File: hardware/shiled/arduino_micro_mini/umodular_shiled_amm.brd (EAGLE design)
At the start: 49.8 x 100.1 mm, 22 parts

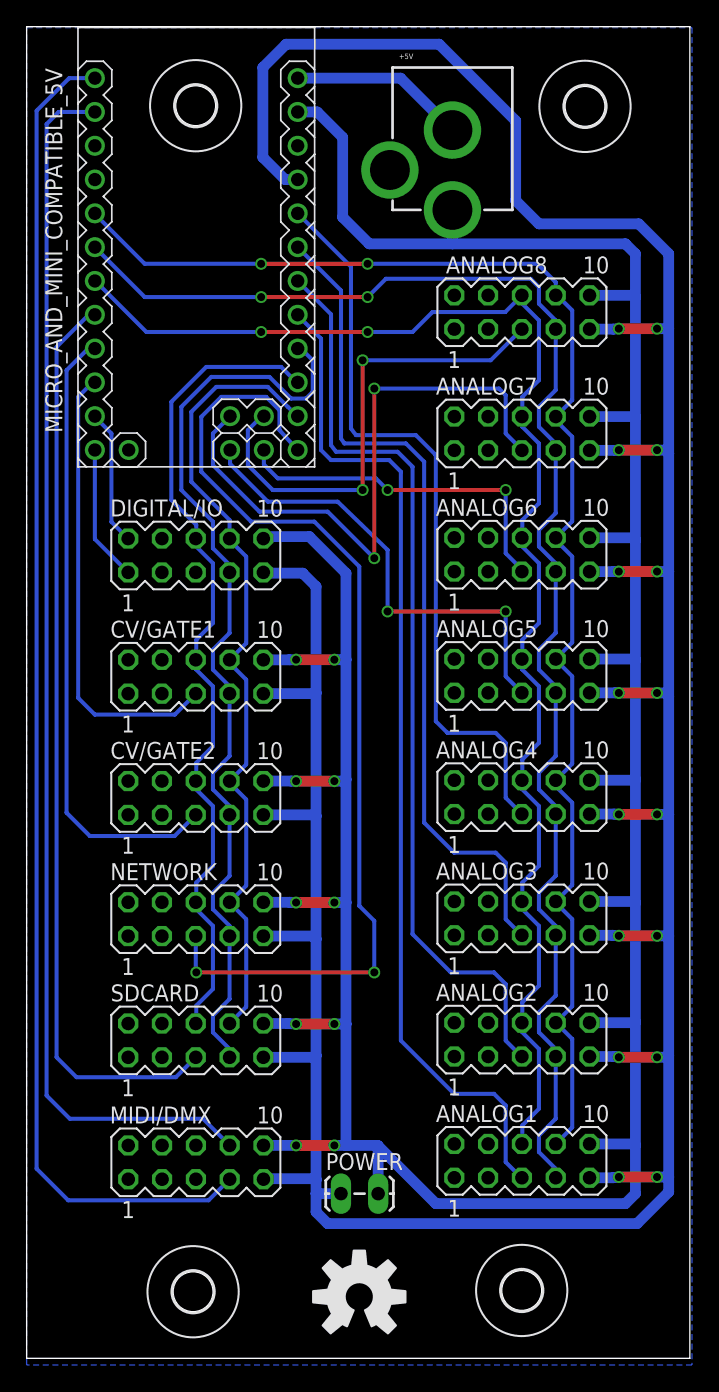
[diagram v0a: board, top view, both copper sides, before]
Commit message: Fix arduino micro/mini shiled size to fixed 10x5cm
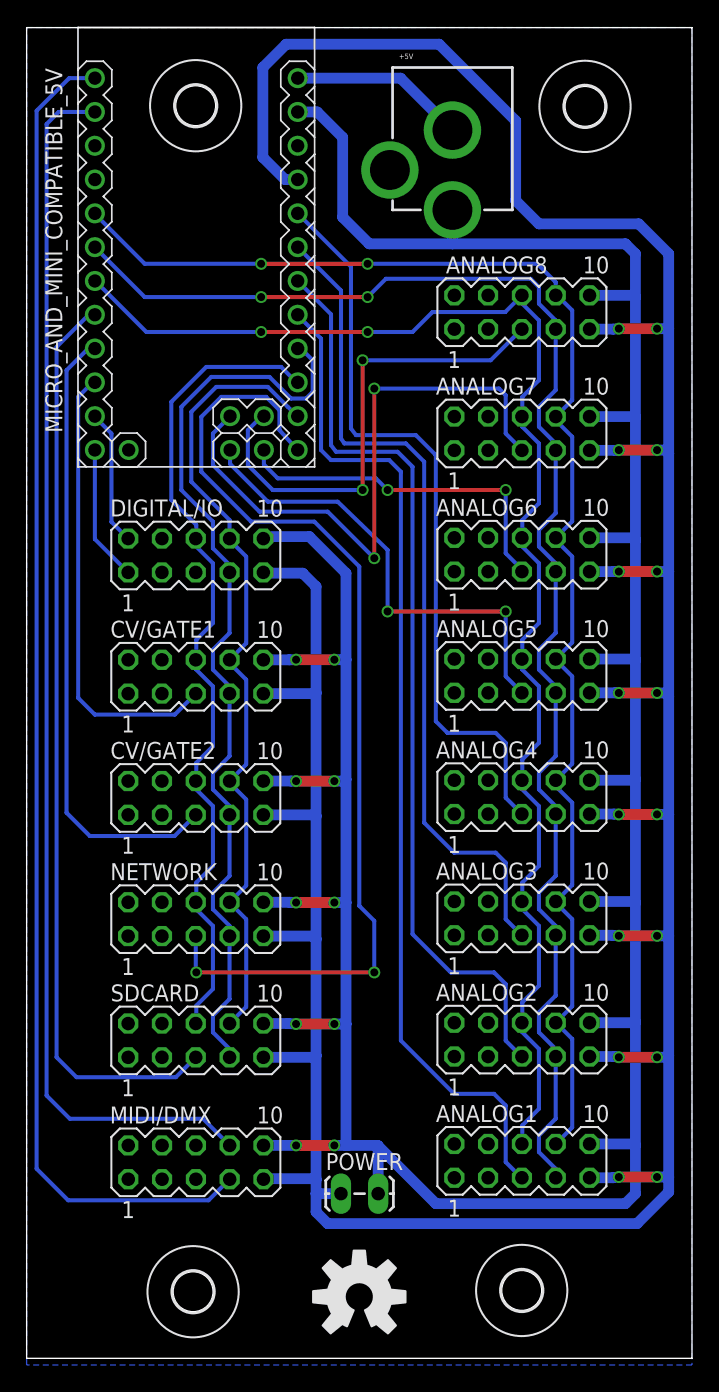
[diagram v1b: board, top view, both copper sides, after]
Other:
- board size 49.8 x 100.1 mm -> 50 x 100 mm
- board text added: "uMODULAR Shield rev. 0.2 CC-BY-SA 4 Romulo Silva http://midilab.co"
- board text removed: "uMODULAR Shield rev. 0.1 CC-BY-SA 4 Romulo Silva http://midilab.co"
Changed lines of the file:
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@@
 <board>
 <plain>
-<wire x1="0" y1="0" x2="49.84" y2="0" width="0" layer="20"/>
-<wire x1="49.84" y1="0" x2="49.84" y2="100.07" width="0" layer="20"/>
-<wire x1="49.84" y1="100.07" x2="0" y2="100.07" width="0" layer="20"/>
-<wire x1="0" y1="100.07" x2="0" y2="0" width="0" layer="20"/>
+<wire x1="0" y1="0" x2="50" y2="0" width="0" layer="20"/>
+<wire x1="50" y1="0" x2="50" y2="100" width="0" layer="20"/>
+<wire x1="50" y1="100" x2="0" y2="100" width="0" layer="20"/>
+<wire x1="0" y1="100" x2="0" y2="0" width="0" layer="20"/>
 <text x="31" y="1.375" size="1.016" layer="26" font="vector" rot="MR0">uMODULAR
-Shield rev. 0.1
+Shield rev. 0.2
 CC-BY-SA 4
 Romulo Silva
